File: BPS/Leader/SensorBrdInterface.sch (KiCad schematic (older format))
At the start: 15 parts, among them J6 MinionConn, J7 CurrentConn, U5 LTC6820, U6 LTC6820, U7 HX1188FNL

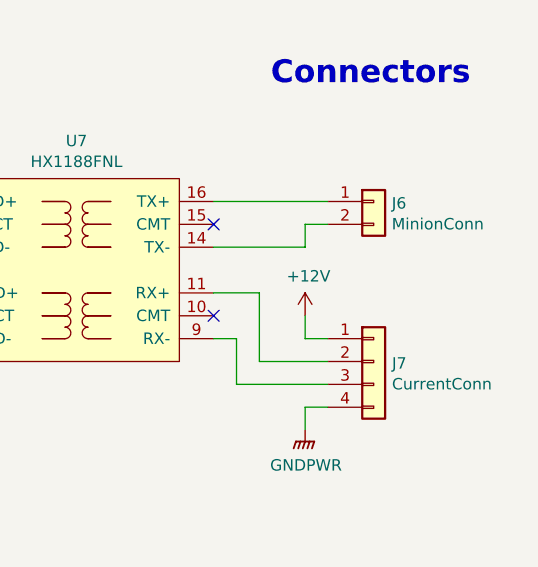
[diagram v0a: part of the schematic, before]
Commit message: Places most components of leader board in their respective locations with nothing traced
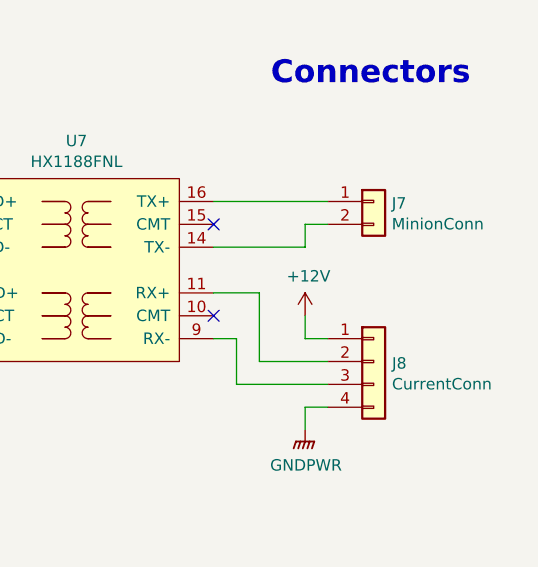
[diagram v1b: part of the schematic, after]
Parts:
- J8: renamed from J7; footprint Connector_Molex:Molex_Micro-Fit_3.0_43650-0415_1x04_P3.00mm_Vertical -> UTSVT_Connectors:Molex_MicroFit3.0_1x4xP3.00mm_PolarizingPeg_Vertical
- renumbered J6 to J7
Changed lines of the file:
@@
 P 9400 3500
 AR Path="/5C4C7509/5D76E59D" Ref="J?"  Part="1"
-AR Path="/5D766247/5D76E59D" Ref="J6"  Part="1"
-F 0 "J6" H 9479 3492 50  0000 L CNN
+AR Path="/5D766247/5D76E59D" Ref="J7"  Part="1"
+F 0 "J7" H 9479 3492 50  0000 L CNN
 F 1 "MinionConn" H 9479 3401 50  0000 L CNN
 F 2 "UTSVT_Connectors:Molex_MicroFit3.0_1x2xP3.00mm_PolarizingPeg_Vertical" H 9400 3500 50  0001 C CNN
@@
 VT: Voltage/Temperature\nI: Current (Amperes)
 $Comp
-L Connector_Generic:Conn_01x04 J7
+L Connector_Generic:Conn_01x04 J8
 U 1 1 5F1F64D7
 P 9400 4200
-F 0 "J7" H 9480 4192 50  0000 L CNN
+F 0 "J8" H 9480 4192 50  0000 L CNN
 F 1 "CurrentConn" H 9480 4101 50  0000 L CNN
-F 2 "Connector_Molex:Molex_Micro-Fit_3.0_43650-0415_1x04_P3.00mm_Vertical" H 9400 4200 50  0001 C CNN
+F 2 "UTSVT_Connectors:Molex_MicroFit3.0_1x4xP3.00mm_PolarizingPeg_Vertical" H 9400 4200 50  0001 C CNN
 F 3 "~" H 9400 4200 50  0001 C CNN
 	1    9400 4200

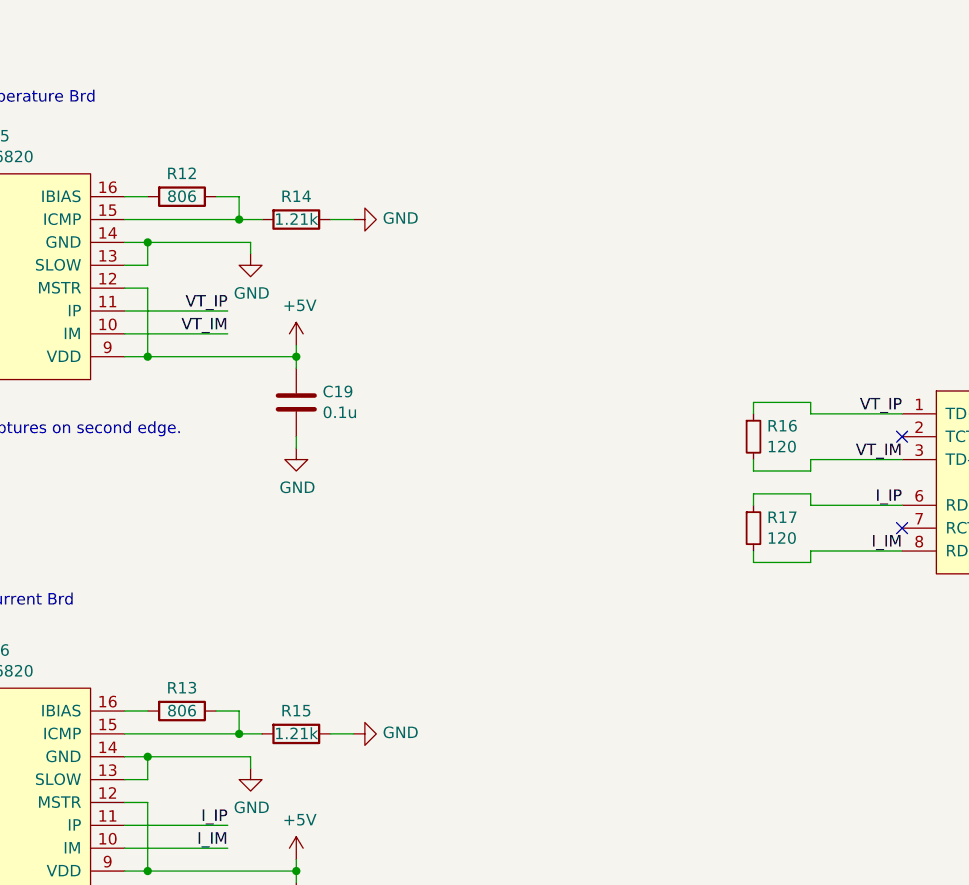
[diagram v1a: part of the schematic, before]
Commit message: Adds power planes
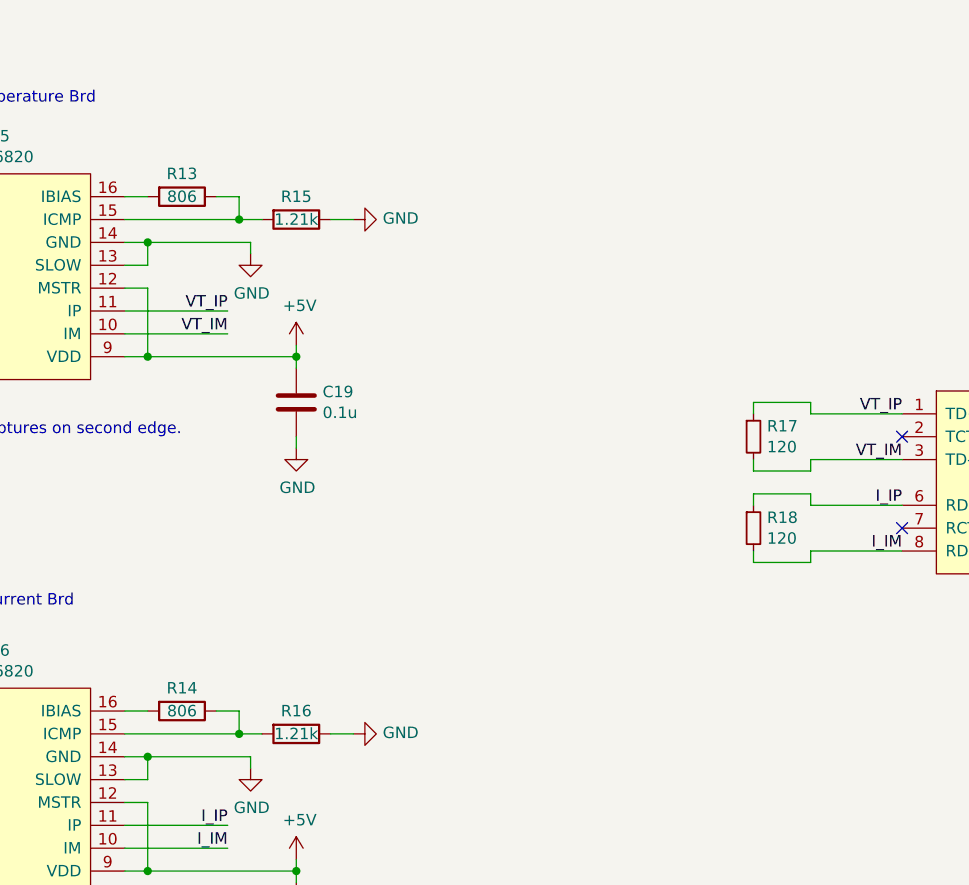
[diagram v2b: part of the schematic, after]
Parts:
- renumbered R12 to R13, R13 to R14, R14 to R15, R15 to R16, R16 to R17, R17 to R18
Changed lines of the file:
@@
 P 4350 2550
 AR Path="/5C4C7509/5D76E57D" Ref="R?"  Part="1"
-AR Path="/5D766247/5D76E57D" Ref="R12"  Part="1"
-F 0 "R12" V 4250 2550 50  0000 C CNN
+AR Path="/5D766247/5D76E57D" Ref="R13"  Part="1"
+F 0 "R13" V 4250 2550 50  0000 C CNN
 F 1 "806" V 4350 2550 50  0000 C CNN
 F 2 "Resistor_SMD:R_0805_2012Metric" V 4280 2550 50  0001 C CNN
@@
 P 4850 2650
 AR Path="/5C4C7509/5D76E587" Ref="R?"  Part="1"
-AR Path="/5D766247/5D76E587" Ref="R14"  Part="1"
-F 0 "R14" V 4750 2650 50  0000 C CNN
+AR Path="/5D766247/5D76E587" Ref="R15"  Part="1"
+F 0 "R15" V 4750 2650 50  0000 C CNN
 F 1 "1.21k" V 4850 2650 50  0000 C CNN
 F 2 "Resistor_SMD:R_0805_2012Metric" V 4780 2650 50  0001 C CNN
@@
 P 6850 3600
 AR Path="/5C4C7509/5D76E5C3" Ref="R?"  Part="1"
-AR Path="/5D766247/5D76E5C3" Ref="R16"  Part="1"
-F 0 "R16" H 6909 3646 50  0000 L CNN
+AR Path="/5D766247/5D76E5C3" Ref="R17"  Part="1"
+F 0 "R17" H 6909 3646 50  0000 L CNN
 F 1 "120" H 6909 3555 50  0000 L CNN
 F 2 "Resistor_SMD:R_0805_2012Metric" H 6850 3600 50  0001 C CNN
@@
 P 6850 4000
 AR Path="/5C4C7509/5F148A8B" Ref="R?"  Part="1"
-AR Path="/5D766247/5F148A8B" Ref="R17"  Part="1"
-F 0 "R17" H 6909 4046 50  0000 L CNN
+AR Path="/5D766247/5F148A8B" Ref="R18"  Part="1"
+F 0 "R18" H 6909 4046 50  0000 L CNN
 F 1 "120" H 6909 3955 50  0000 L CNN
 F 2 "Resistor_SMD:R_0805_2012Metric" H 6850 4000 50  0001 C CNN
@@
 P 4350 4800
 AR Path="/5C4C7509/5F151EAD" Ref="R?"  Part="1"
-AR Path="/5D766247/5F151EAD" Ref="R13"  Part="1"
-F 0 "R13" V 4250 4800 50  0000 C CNN
+AR Path="/5D766247/5F151EAD" Ref="R14"  Part="1"
+F 0 "R14" V 4250 4800 50  0000 C CNN
 F 1 "806" V 4350 4800 50  0000 C CNN
 F 2 "Resistor_SMD:R_0805_2012Metric" V 4280 4800 50  0001 C CNN
@@
 P 4850 4900
 AR Path="/5C4C7509/5F151EB7" Ref="R?"  Part="1"
-AR Path="/5D766247/5F151EB7" Ref="R15"  Part="1"
-F 0 "R15" V 4750 4900 50  0000 C CNN
+AR Path="/5D766247/5F151EB7" Ref="R16"  Part="1"
+F 0 "R16" V 4750 4900 50  0000 C CNN
 F 1 "1.21k" V 4850 4900 50  0000 C CNN
 F 2 "Resistor_SMD:R_0805_2012Metric" V 4780 4900 50  0001 C CNN

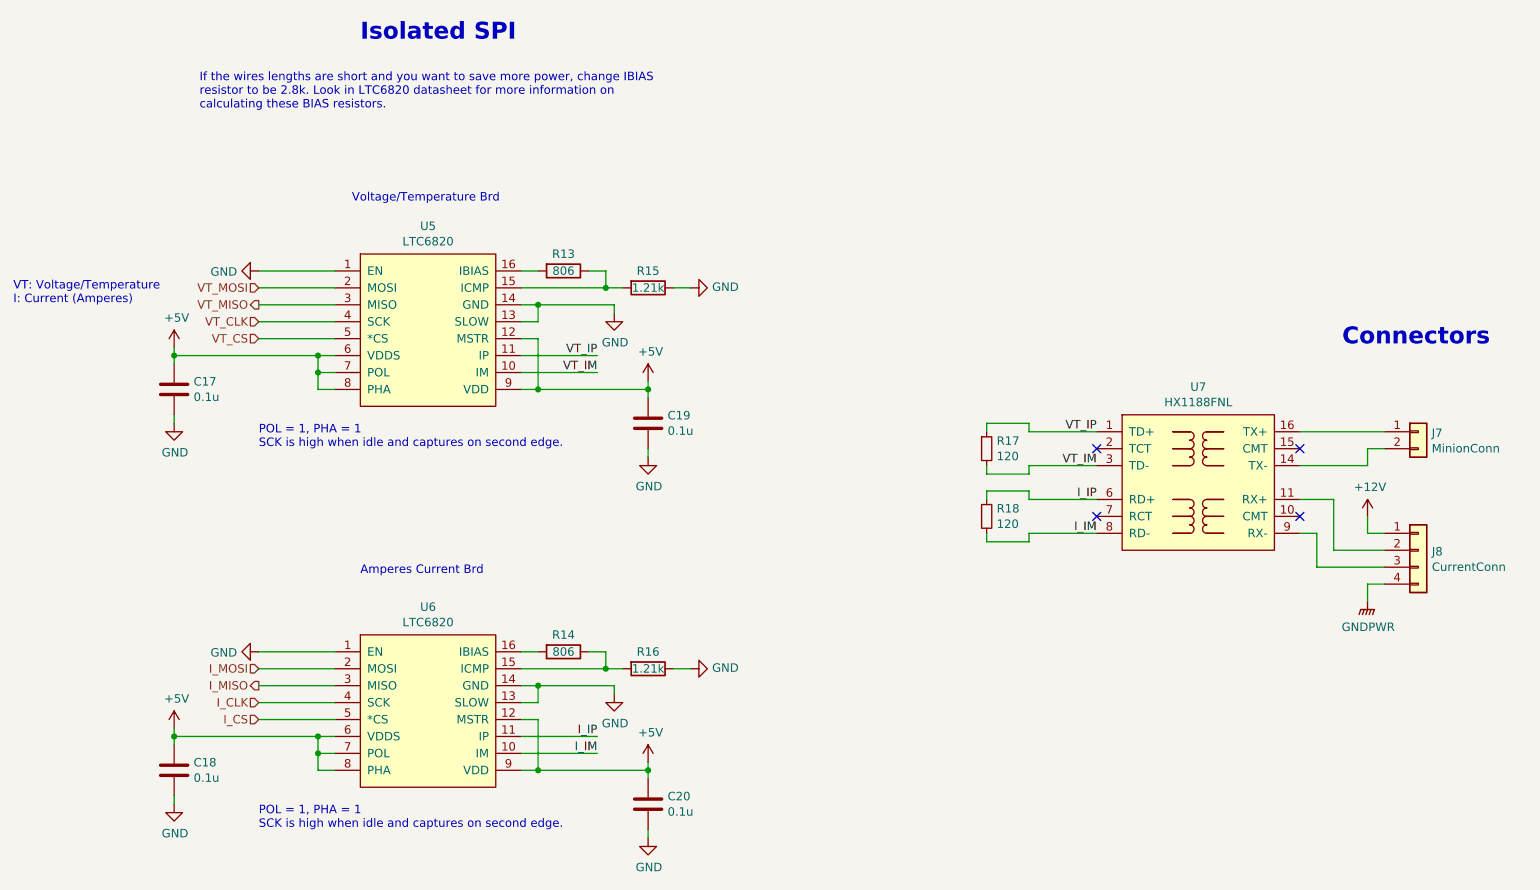
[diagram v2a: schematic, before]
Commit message: Finished leader board
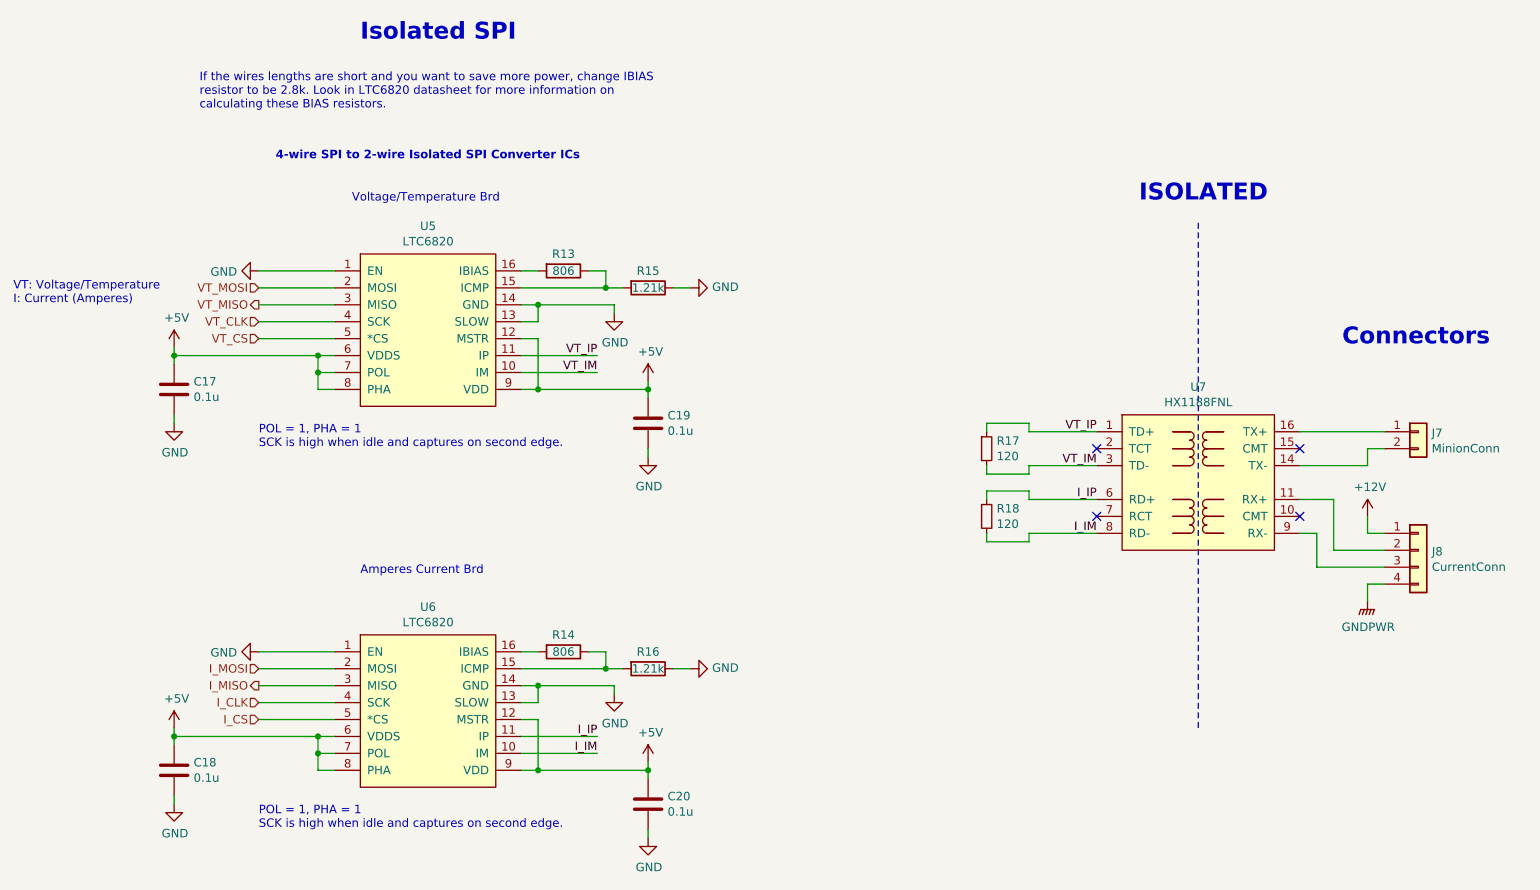
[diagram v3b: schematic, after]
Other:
- note added: "4-wire SPI to 2-wire Isolated SPI Converter ICs"
- note added: "ISOLATED"
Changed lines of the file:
@@
 	1    0    0    -1
 $EndComp
+Wire Notes Line
+	8100 5250 8100 2250
+Text Notes 7750 2150 0    100  ~ 20
+ISOLATED
+Text Notes 2650 1900 0    50   ~ 10
+4-wire SPI to 2-wire Isolated SPI Converter ICs
 $EndSCHEMATC
